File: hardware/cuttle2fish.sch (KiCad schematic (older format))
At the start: 11 parts

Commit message: Update cuttle2fish.sch
Add labels for pins we want to break out and programming connector
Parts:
- added J?: CONN_01X05, symbol CONN_01X05
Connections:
- net labels added: BUTTON, RESET, SPI1_MISO, SPI1_MOSI, SPI1_SCK, USART1_RX, USART1_TX
- wire segments 41 -> 54
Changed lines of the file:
@@
 LIBS:valves
 LIBS:stm32
+LIBS:cuttle2fish-cache
 EELAYER 26 0
 EELAYER END
@@
 	1000 5100 1000 4400
 Wire Wire Line
-	1000 4400 2600 4400
+	900  4400 2600 4400
 Wire Wire Line
 	750  4300 750  5400
@@
 Text Label 1600 2300 0    60   ~ 0
 USB_DP
+$Comp
+L CONN_01X05 J?
+U 1 1 5BF8A16C
+P 2200 6400
+F 0 "J?" H 2278 6441 50  0000 L CNN
+F 1 "CONN_01X05" H 2278 6350 50  0000 L CNN
+F 2 "" H 2200 6400 50  0001 C CNN
+F 3 "" H 2200 6400 50  0001 C CNN
+	1    2200 6400
+	1    0    0    -1
+$EndComp
+Wire Wire Line
+	1600 6200 2000 6200
+Wire Wire Line
+	2000 6300 1600 6300
+Wire Wire Line
+	2000 6400 1600 6400
+Wire Wire Line
+	2000 6500 1600 6500
+Wire Wire Line
+	2000 6600 1600 6600
+Wire Wire Line
+	1600 6200 1600 6150
+Wire Wire Line
+	1600 6600 1600 6650
+$Comp
+L GND #PWR?
+U 1 1 5BF8A428
+P 1600 6650
+F 0 "#PWR?" H 1600 6400 50  0001 C CNN
+F 1 "GND" H 1605 6477 50  0000 C CNN
+F 2 "" H 1600 6650 50  0001 C CNN
+F 3 "" H 1600 6650 50  0001 C CNN
+	1    1600 6650
+	1    0    0    -1
+$EndComp
+$Comp
+L +3V3 #PWR?
+U 1 1 5BF8A477
+P 1600 6150
+F 0 "#PWR?" H 1600 6000 50  0001 C CNN
+F 1 "+3V3" H 1615 6323 50  0000 C CNN
+F 2 "" H 1600 6150 50  0001 C CNN
+F 3 "" H 1600 6150 50  0001 C CNN
+	1    1600 6150
+	1    0    0    -1
+$EndComp
+Connection ~ 1000 4400
+Text Label 900  4400 0    60   ~ 0
+RESET
+Text Label 1600 6500 0    60   ~ 0
+RESET
+Text Label 1600 6400 0    60   ~ 0
+SWDIO
+Text Label 1600 6300 0    60   ~ 0
+SWCLK
+Wire Wire Line
+	9400 1200 9550 1200
+Wire Wire Line
+	9400 1300 9550 1300
+Wire Wire Line
+	9400 1500 9550 1500
+Wire Wire Line
+	9400 1600 9550 1600
+Wire Wire Line
+	9400 1400 9550 1400
+Text Label 9550 1200 0    60   ~ 0
+SPI1_SCK
+Text Label 9550 1300 0    60   ~ 0
+SPI1_MISO
+Text Label 9550 1400 0    60   ~ 0
+SPI1_MOSI
+Text Label 9550 1500 0    60   ~ 0
+USART1_TX
+Text Label 9550 1600 0    60   ~ 0
+USART1_RX
+Wire Wire Line
+	9400 1700 9550 1700
+Text Label 9550 1700 0    60   ~ 0
+BUTTON
 $EndSCHEMATC

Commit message: Add APA102, button, PMIC
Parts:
- removed J?: USB_A, symbol USB_A
- added C?: 10nF, symbol Device:C_Small
- added C? (x2): 4.7uF, symbol Device:C_Small
- added J?: USB_A, symbol Connector:USB_A
- added R?: R_Small, symbol Device:R_Small
- added SW?: SW_Push_Dual, symbol Switch:SW_Push_Dual
- added U?: LP2985-3.3, Package_TO_SOT_SMD:SOT-23-5, symbol Regulator_Linear:LP2985-3.3
- added U? (x2): APA102-2020, symbol cuttle2fish-cache:APA102_2020
- C? (x2): value C_Small -> 20pF; symbol C_Small -> Device:C_Small
- C? (x5): value ?? -> 100nF; symbol C_Small -> Device:C_Small
- C?: value C_Small -> 100nF; symbol C_Small -> Device:C_Small
- J?: symbol CONN_01X05 -> Connector:Conn_01x05_Female
- U?: symbol STM32F103R(8-B)Tx -> stm321:STM32F103R(8-B)Tx
- Y?: value Crystal -> 8 MHz; symbol Crystal -> Device:Crystal
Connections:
- net labels added: +5V
- net labels removed: VBUS
- wire segments 54 -> 114
- no-connect marks 0 -> 2

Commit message: Rev 1 schematic
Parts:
- added J3: Conn_01x05, symbol Connector:Conn_01x05_Female
- R1: renamed from R?; value R_Small -> 10K
- U3, U4: renamed from U?; symbol cuttle2fish-cache:APA102_2020 -> test:APA102_2020
- gave numbers to parts that had none: 17
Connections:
- net labels added: PB0, PB1
- net labels removed: SPI1_MISO
- wire segments 114 -> 121
- no-connect marks 2 -> 40
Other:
- moved on the sheet: J2

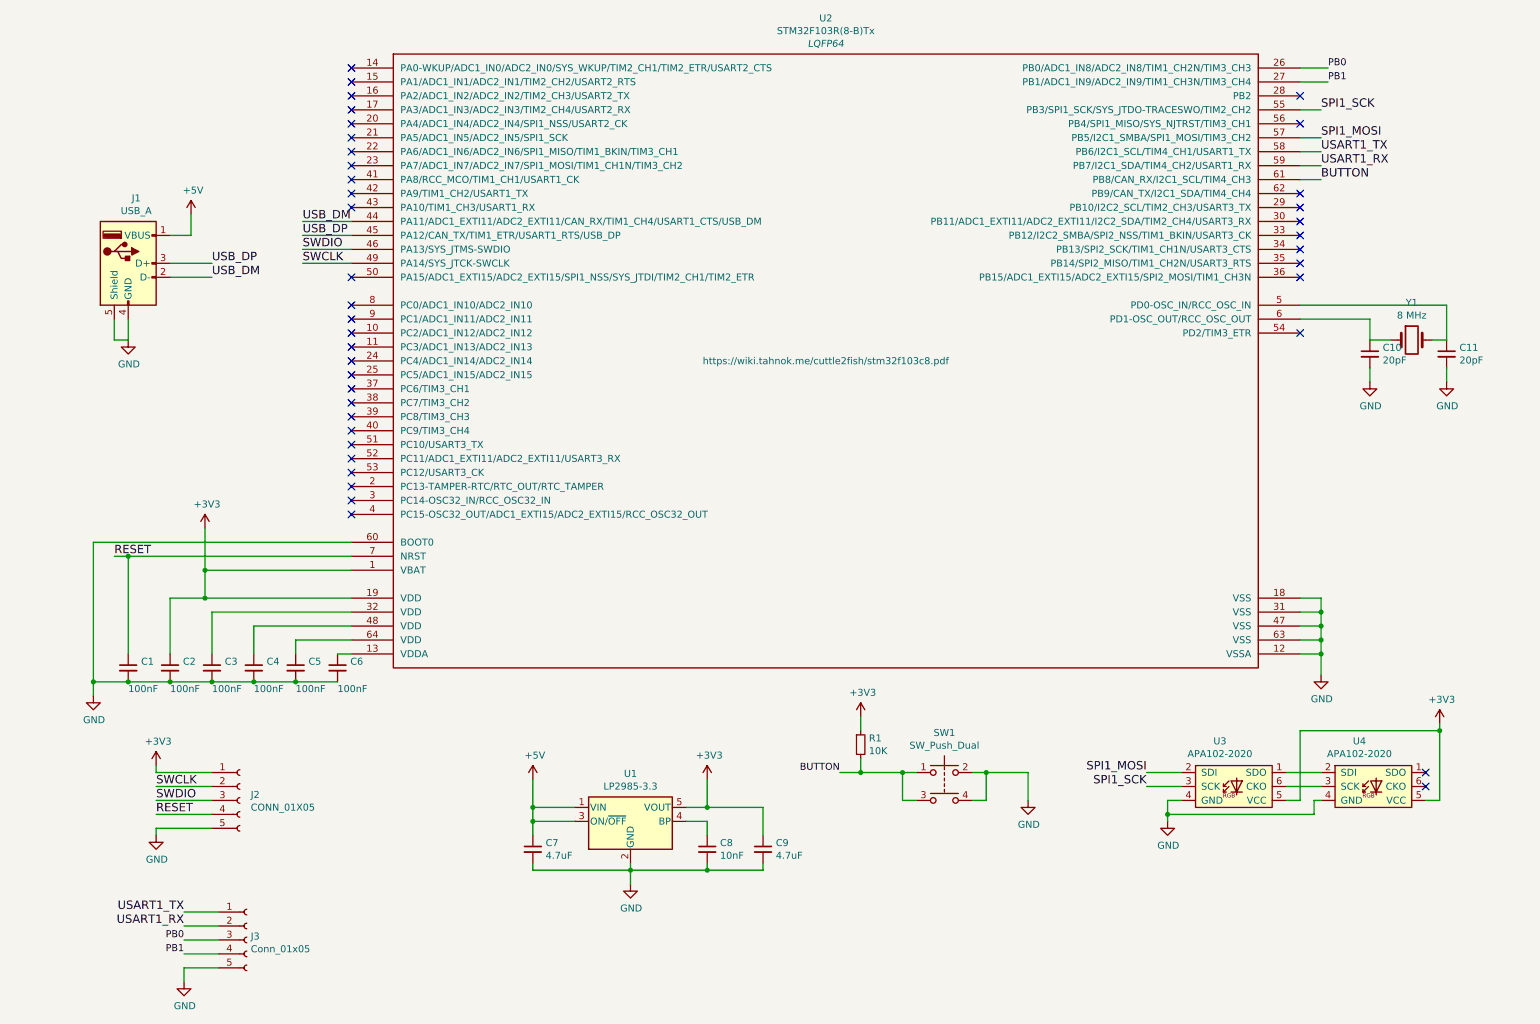
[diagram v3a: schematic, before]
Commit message: Add APA102 footprint from great scott gadgets
https://github.com/greatscottgadgets/gsg-kicad-lib/blob/master/gsg-modules.pretty/APA102-2020.kicad_mod
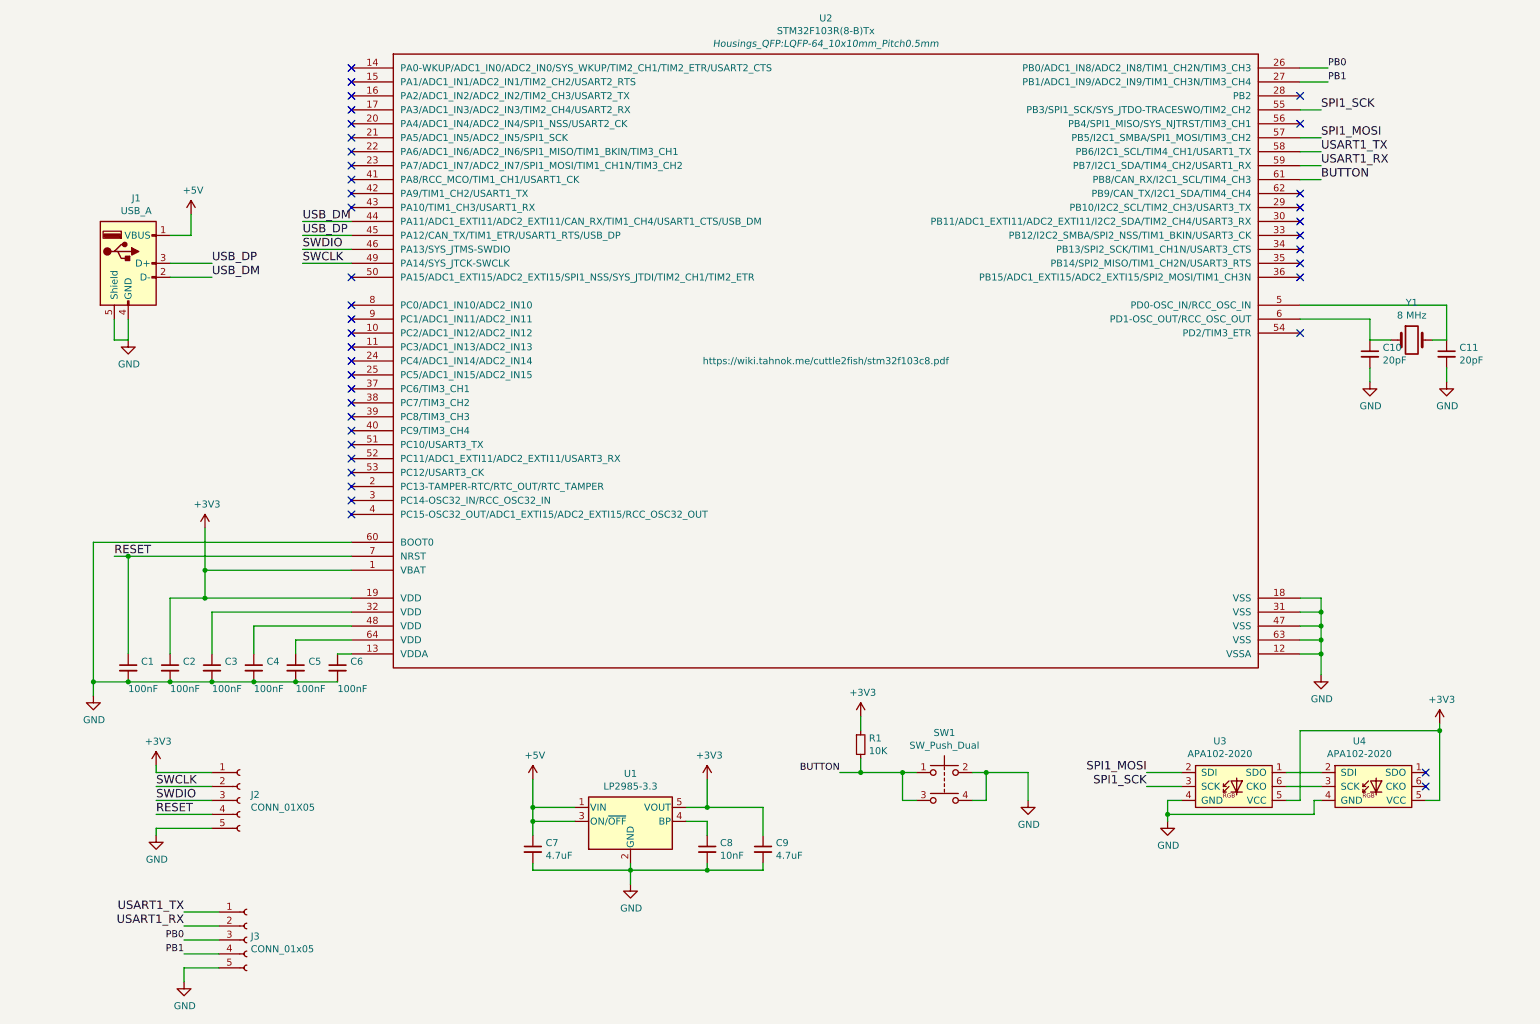
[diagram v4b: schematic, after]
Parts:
- C1, C10, C11, C2, C3, C4, C5, C6, C7, C8, C9: footprint (none) -> Capacitors_SMD:C_0603
- J2: footprint (none) -> Socket_Strips:Socket_Strip_Straight_1x05_Pitch2.54mm
- J3: value Conn_01x05 -> CONN_01x05; footprint (none) -> Socket_Strips:Socket_Strip_Straight_1x05_Pitch2.54mm
- R1: footprint (none) -> Resistors_SMD:R_0603
- U1: footprint Package_TO_SOT_SMD:SOT-23-5 -> TO_SOT_Packages_SMD:SOT-23-5
- U2: footprint LQFP64 -> Housings_QFP:LQFP-64_10x10mm_Pitch0.5mm
- U3, U4: footprint (none) -> footprints:APA102-2020
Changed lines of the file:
@@
 F 0 "U2" H 6000 5457 50  0000 C CNN
 F 1 "STM32F103R(8-B)Tx" H 6000 5366 50  0000 C CNN
-F 2 "LQFP64" H 6000 5275 50  0000 C CIN
+F 2 "Housings_QFP:LQFP-64_10x10mm_Pitch0.5mm" H 6000 5275 50  0000 C CIN
 F 3 "https://wiki.tahnok.me/cuttle2fish/stm32f103c8.pdf" H 6000 3000 50  0000 C CNN
 	1    6000 3000
@@
 F 0 "C11" H 10542 2996 50  0000 L CNN
 F 1 "20pF" H 10542 2905 50  0000 L CNN
-F 2 "" H 10450 2950 50  0001 C CNN
+F 2 "Capacitors_SMD:C_0603" H 10450 2950 50  0001 C CNN
 F 3 "" H 10450 2950 50  0001 C CNN
 	1    10450 2950
@@
 F 0 "C10" H 9992 2996 50  0000 L CNN
 F 1 "20pF" H 9992 2905 50  0000 L CNN
-F 2 "" H 9900 2950 50  0001 C CNN
+F 2 "Capacitors_SMD:C_0603" H 9900 2950 50  0001 C CNN
 F 3 "" H 9900 2950 50  0001 C CNN
 	1    9900 2950
@@
 F 0 "C6" H 2592 5246 50  0000 L CNN
 F 1 "100nF" H 2500 5050 50  0000 L CNN
-F 2 "" H 2500 5200 50  0001 C CNN
+F 2 "Capacitors_SMD:C_0603" H 2500 5200 50  0001 C CNN
 F 3 "" H 2500 5200 50  0001 C CNN
 	1    2500 5200
@@
 F 0 "C5" H 2292 5246 50  0000 L CNN
 F 1 "100nF" H 2200 5050 50  0000 L CNN
-F 2 "" H 2200 5200 50  0001 C CNN
+F 2 "Capacitors_SMD:C_0603" H 2200 5200 50  0001 C CNN
 F 3 "" H 2200 5200 50  0001 C CNN
 	1    2200 5200
@@
 F 0 "C4" H 1992 5246 50  0000 L CNN
 F 1 "100nF" H 1900 5050 50  0000 L CNN
-F 2 "" H 1900 5200 50  0001 C CNN
+F 2 "Capacitors_SMD:C_0603" H 1900 5200 50  0001 C CNN
 F 3 "" H 1900 5200 50  0001 C CNN
 	1    1900 5200
@@
 F 0 "C3" H 1692 5246 50  0000 L CNN
 F 1 "100nF" H 1600 5050 50  0000 L CNN
-F 2 "" H 1600 5200 50  0001 C CNN
+F 2 "Capacitors_SMD:C_0603" H 1600 5200 50  0001 C CNN
 F 3 "" H 1600 5200 50  0001 C CNN
 	1    1600 5200
@@
 F 0 "C2" H 1392 5246 50  0000 L CNN
 F 1 "100nF" H 1300 5050 50  0000 L CNN
-F 2 "" H 1300 5200 50  0001 C CNN
+F 2 "Capacitors_SMD:C_0603" H 1300 5200 50  0001 C CNN
 F 3 "" H 1300 5200 50  0001 C CNN
 	1    1300 5200
@@
 F 0 "C1" H 1092 5246 50  0000 L CNN
 F 1 "100nF" H 1000 5050 50  0000 L CNN
-F 2 "" H 1000 5200 50  0001 C CNN
+F 2 "Capacitors_SMD:C_0603" H 1000 5200 50  0001 C CNN
 F 3 "" H 1000 5200 50  0001 C CNN
 	1    1000 5200
@@
 F 0 "J2" H 1878 6191 50  0000 L CNN
 F 1 "CONN_01X05" H 1878 6100 50  0000 L CNN
-F 2 "" H 1800 6150 50  0001 C CNN
+F 2 "Socket_Strips:Socket_Strip_Straight_1x05_Pitch2.54mm" H 1800 6150 50  0001 C CNN
 F 3 "" H 1800 6150 50  0001 C CNN
 	1    1800 6150
@@
 F 0 "U1" H 4600 6642 50  0000 C CNN
 F 1 "LP2985-3.3" H 4600 6551 50  0000 C CNN
-F 2 "Package_TO_SOT_SMD:SOT-23-5" H 4600 6625 50  0001 C CNN
+F 2 "TO_SOT_Packages_SMD:SOT-23-5" H 4600 6625 50  0001 C CNN
 F 3 "http://www.ti.com/lit/ds/symlink/lp2985.pdf" H 4600 6300 50  0001 C CNN
 	1    4600 6300
@@
 F 0 "C8" H 5242 6546 50  0000 L CNN
 F 1 "10nF" H 5242 6455 50  0000 L CNN
-F 2 "" H 5150 6500 50  0001 C CNN
+F 2 "Capacitors_SMD:C_0603" H 5150 6500 50  0001 C CNN
 F 3 "~" H 5150 6500 50  0001 C CNN
 	1    5150 6500
@@
 F 0 "C9" H 5642 6546 50  0000 L CNN
 F 1 "4.7uF" H 5642 6455 50  0000 L CNN
-F 2 "" H 5550 6500 50  0001 C CNN
+F 2 "Capacitors_SMD:C_0603" H 5550 6500 50  0001 C CNN
 F 3 "~" H 5550 6500 50  0001 C CNN
 	1    5550 6500
@@
 F 0 "C7" H 3992 6546 50  0000 L CNN
 F 1 "4.7uF" H 3992 6455 50  0000 L CNN
-F 2 "" H 3900 6500 50  0001 C CNN
+F 2 "Capacitors_SMD:C_0603" H 3900 6500 50  0001 C CNN
 F 3 "~" H 3900 6500 50  0001 C CNN
 	1    3900 6500
@@
 F 0 "R1" H 6309 5796 50  0000 L CNN
 F 1 "10K" H 6309 5705 50  0000 L CNN
-F 2 "" H 6250 5750 50  0001 C CNN
+F 2 "Resistors_SMD:R_0603" H 6250 5750 50  0001 C CNN
 F 3 "~" H 6250 5750 50  0001 C CNN
 	1    6250 5750
@@
 F 0 "U3" H 8825 5975 50  0000 C CNN
 F 1 "APA102-2020" H 8825 5884 50  0000 C CNN
-F 2 "" H 8750 5850 50  0001 C CNN
+F 2 "footprints:APA102-2020" H 8750 5850 50  0001 C CNN
 F 3 "http://www.led-color.com/upload/201604/APA102-2020%20SMD%20LED.pdf" H 8750 5850 50  0001 C CNN
 	1    8750 5850
@@
 F 0 "U4" H 9825 5975 50  0000 C CNN
 F 1 "APA102-2020" H 9825 5884 50  0000 C CNN
-F 2 "" H 9750 5850 50  0001 C CNN
+F 2 "footprints:APA102-2020" H 9750 5850 50  0001 C CNN
 F 3 "http://www.led-color.com/upload/201604/APA102-2020%20SMD%20LED.pdf" H 9750 5850 50  0001 C CNN
 	1    9750 5850
@@
 P 1850 7150
 F 0 "J3" H 1878 7176 50  0000 L CNN
-F 1 "Conn_01x05" H 1878 7085 50  0000 L CNN
-F 2 "" H 1850 7150 50  0001 C CNN
+F 1 "CONN_01x05" H 1878 7085 50  0000 L CNN
+F 2 "Socket_Strips:Socket_Strip_Straight_1x05_Pitch2.54mm" H 1850 7150 50  0001 C CNN
 F 3 "~" H 1850 7150 50  0001 C CNN
 	1    1850 7150

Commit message: Add LEDs and button footprint
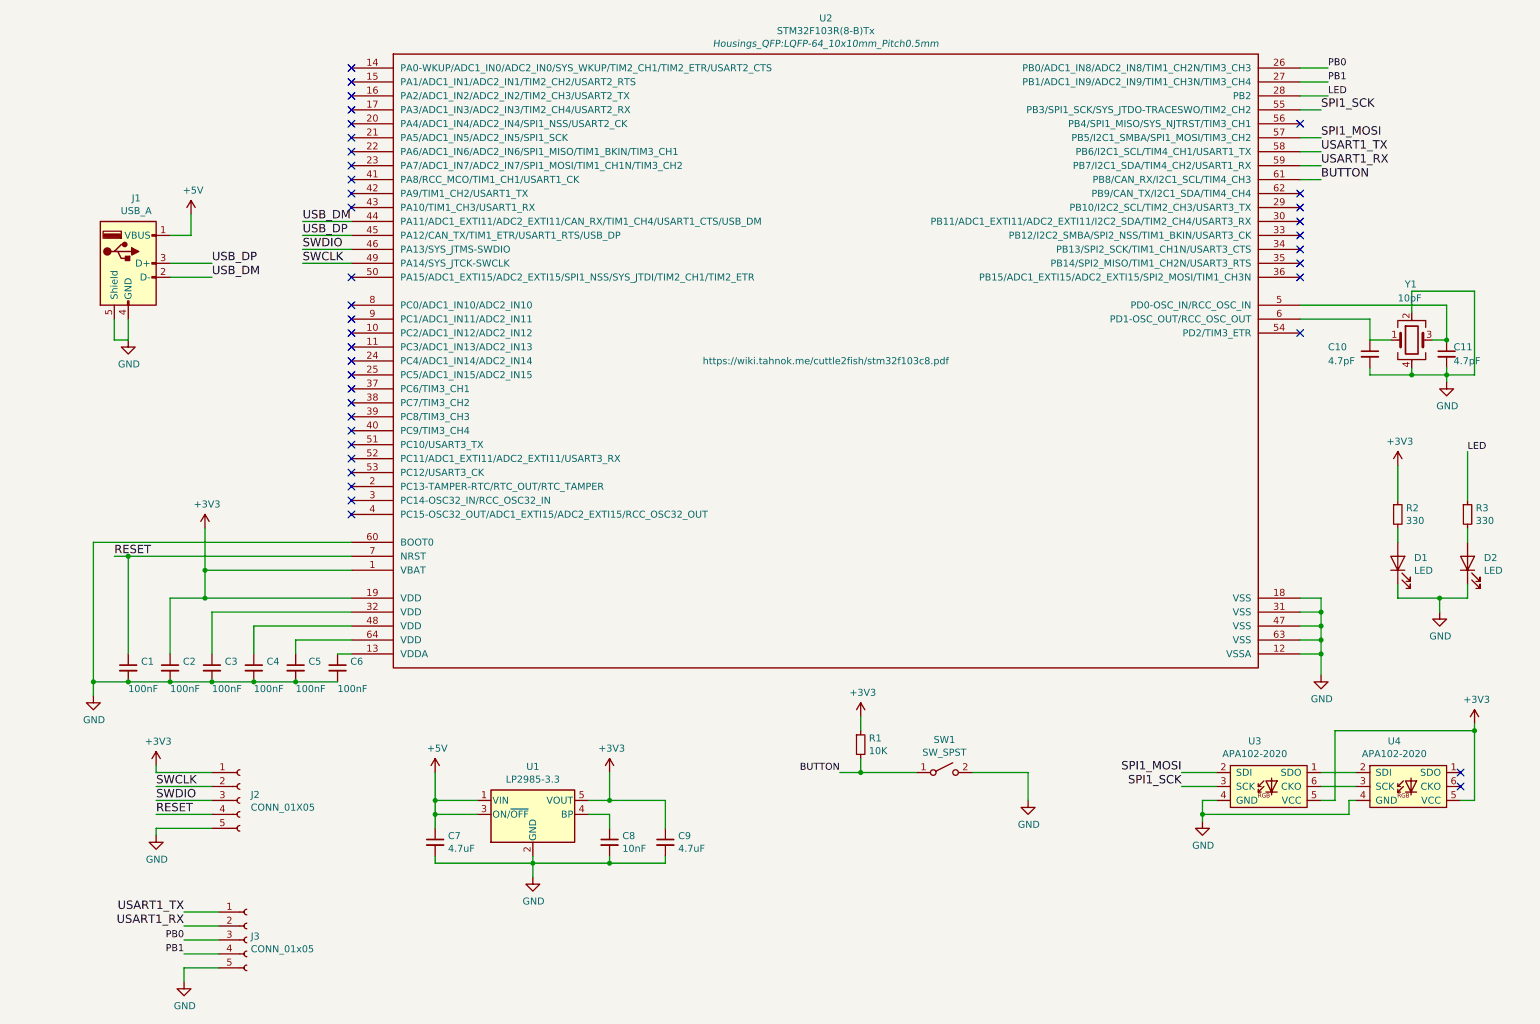
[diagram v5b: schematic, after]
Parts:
- removed SW1: SW_Push_Dual, symbol Switch:SW_Push_Dual
- removed Y1: 8 MHz, symbol Device:Crystal
- added D1, D2: LED, LEDs:LED_0603, symbol Device:LED
- added R2, R3: 330, Resistors_SMD:R_0603, symbol Device:R_Small
- added SW1: SW_SPST, Buttons_Switches_SMD:SW_SPST_B3U-1000P, symbol Switch:SW_SPST
- added Y1: 10pF, Crystals:Crystal_SMD_5032-4pin_5.0x3.2mm, symbol Device:Crystal_GND24
- C10, C11: value 20pF -> 4.7pF
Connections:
- net +3V3: now also R2.1
- net BUTTON: now also SW1.1 (A)
- net GND: now also D1.1 (K), D2.1 (K), SW1.2 (B), Y1.2, Y1.4
- net LED: now reaches U2.28 (PB2)
- net LED: now also R3.1
- net at C11.1, U2.5 (PD0-OSC_IN/RCC_OSC_IN): now also Y1.3
- net at C10.1, U2.6 (PD1-OSC_OUT/RCC_OSC_OUT): now also Y1.1
- new net: D1.2 (A), R2.2
- new net: D2.2 (A), R3.2
- no-connect marks 40 -> 39
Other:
- moved on the sheet: C7, C8, C9, U1, U3, U4
